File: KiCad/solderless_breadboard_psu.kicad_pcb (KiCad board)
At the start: 4 copper layers, 55 x 49.8 mm, 87 parts, among them IC301 MCP73831T-2ACI_OT, IC302 BQ29737DSER, IC401 TLV62569DBVR, IC501 FT232RL-REEL, J201 Barrel_Jack_Switch_Pin3Ring, J301 BM02B-GHS-TBT_LF__SN__N_, J501 Conn_01x09_Pin, J502 Conn_01x09_Pin, J503 Conn_01x06_Pin, J504 USB_C_Receptacle_USB2.0_16P, J601 Conn_02x03_Odd_Even, J602 Conn_02x03_Odd_Even, Q301 DMG3415U-7, Q302 T2N7002AK, Q303 T2N7002AK, U401 TPS61040DBVR, U501 USBLC6-2SC6

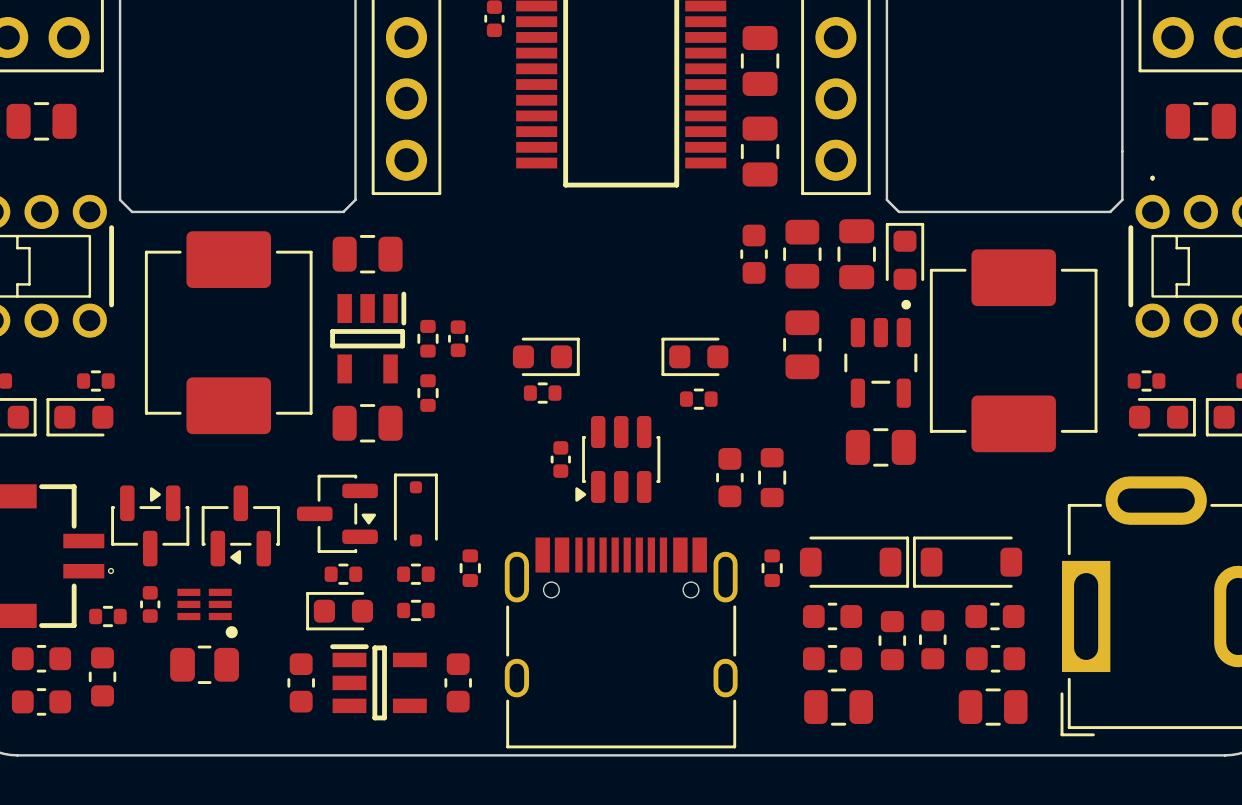
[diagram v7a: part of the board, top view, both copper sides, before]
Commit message: USB routing
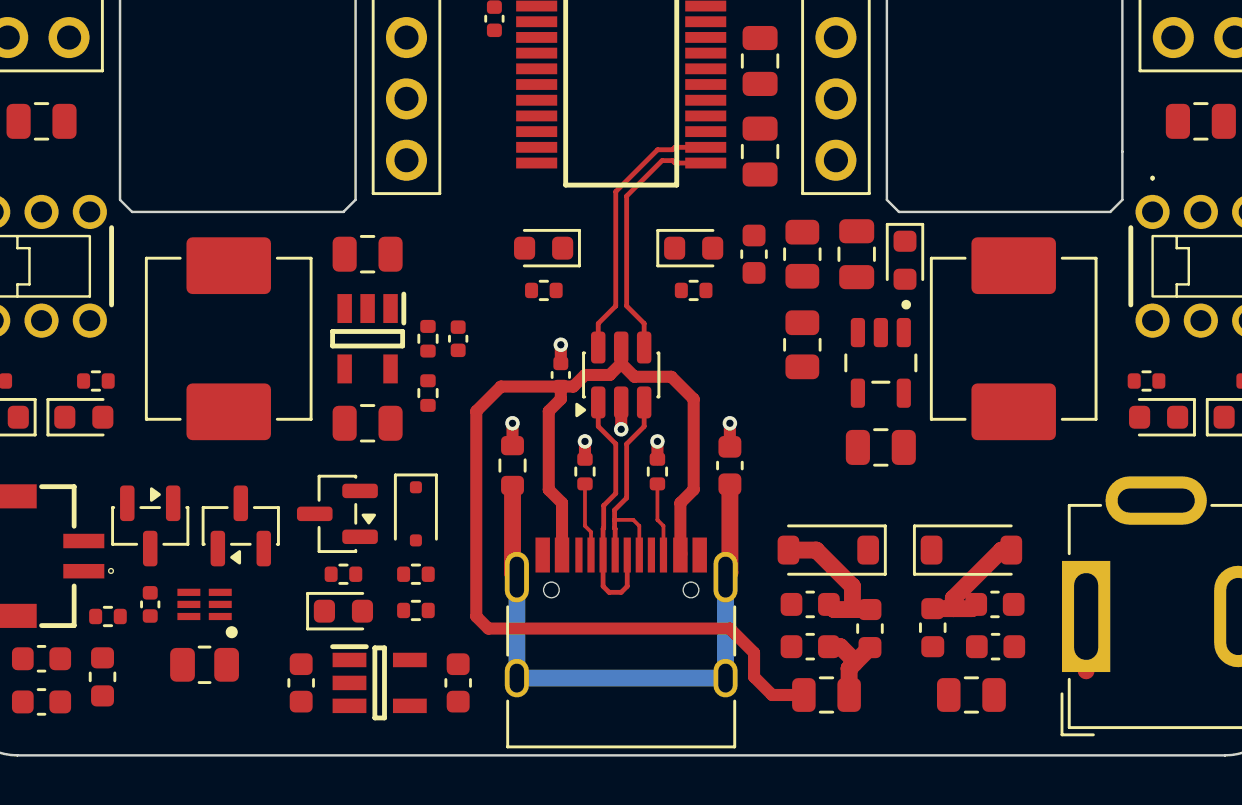
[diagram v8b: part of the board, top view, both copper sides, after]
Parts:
- moved R505 10.8 mm to (45.5, 85.5)
- moved R501 6.21 mm to (48.5, 85.8)
- moved R502 6.21 mm to (51.5, 85.8)
- moved D402 4.51 mm to (53.0, 76.5)
- moved R405 4.51 mm to (53.0, 78.2)
- moved D403 4.50 mm to (46.8, 76.5)
- moved R406 4.25 mm to (46.8, 78.2)
- moved C504 3.50 mm to (47.5, 81.8), turned to 90 degrees
- moved U501 3.50 mm to (50.0, 81.8)
- moved FB202 1.05 mm to (60.3, 92.2)
- moved C203 1.05 mm to (57.8, 93.0)
- moved C204 1.05 mm to (57.8, 91.2)
- moved D202 1.05 mm to (58.6, 89.0)
- moved F201 1.03 mm to (64.5, 95.0)
- moved F202 0.71 mm to (58.5, 95.0)
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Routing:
- net USB2UART_VBUS: track 0.00 -> 49.2 mm
- net GNDPWR: track 0.00 -> 25.0 mm
- net /[5]USB 2 UART/USB2UART_D-: track 0.00 -> 11.2 mm
- net /[5]USB 2 UART/USB2UART_CONN_D-: track 0.00 -> 11.0 mm
- net /[5]USB 2 UART/USB2UART_D+: track 0.00 -> 10.5 mm
- net /[5]USB 2 UART/USB2UART_CONN_D+: track 0.00 -> 9.53 mm
- net +VCC_USB2UART_FILT: track 0.00 -> 6.02 mm
- net +5V_IN_FILT: track 0.00 -> 5.53 mm
- net GND: track 0.00 -> 5.26 mm, vias 0 -> 6
- net +VCC_USB2UART_FUSE: track 0.00 -> 4.04 mm
- net /[5]USB 2 UART/USB2UART_CONN_CC2: track 0.00 -> 3.05 mm
- net /[5]USB 2 UART/USB2UART_CONN_CC1: track 0.00 -> 3.05 mm
- net +5V_BJ: track 0.00 -> 2.25 mm
- added copper zone on In1.Cu, net GND
- added copper zone on In2.Cu, net GND
